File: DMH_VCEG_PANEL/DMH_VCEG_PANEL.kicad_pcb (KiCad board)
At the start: 2 copper layers, 100 x 200 mm, 5 parts, among them J0 Panel_GND_Solder_Wire_Pad

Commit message: 15cm Panel design in progress
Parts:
- added H10: Dec CV, SynthStuff:Pot_Cutout_Tiny_attv_P110KH1, F.Cu at (248.7, 145.7)
- added H11: Sus CV, SynthStuff:Pot_Cutout_Tiny_attv_P110KH1, F.Cu at (274.2, 121.4)
- added H12: Rel CV, SynthStuff:Pot_Cutout_Tiny_attv_P110KH1, F.Cu at (274.2, 145.7)
- added H13: Exp Lin, SynthStuff:Toggle_Switch_TE_Cutout, F.Cu at (243.5, 165.6)
- added H14: Loop, SynthStuff:Toggle_Switch_TE_Cutout, F.Cu at (258.5, 165.6)
- added H15: Att CV, SynthStuff:Jack_6.35mm_Cutout_v3, F.Cu at (33.5, 190.2)
- added H16: Dec CV, SynthStuff:Jack_6.35mm_Cutout_v3, F.Cu at (50.0, 190.2)
- added H17: Sus CV, SynthStuff:Jack_6.35mm_Cutout_v3, F.Cu at (66.5, 190.2)
- added H18: Rel CV, SynthStuff:Jack_6.35mm_Cutout_v3, F.Cu at (83.0, 190.2)
- added H19: Trig, SynthStuff:Jack_6.35mm_Cutout_v3, F.Cu at (83.0, 208.8)
- added H20: Gate, SynthStuff:Jack_6.35mm_Cutout_v3, F.Cu at (66.5, 208.8)
- added H21: Out +, SynthStuff:Jack_6.35mm_Cutout_Output_v6, F.Cu at (33.5, 208.8)
- added H22: Out -, SynthStuff:Jack_6.35mm_Cutout_Output_v6, F.Cu at (50.0, 208.8)
- added H23: SG Out A, SynthStuff:Jack_6.35mm_Cutout_Output_v6, F.Cu at (100.0, 190.2)
- added H24: Att LED, SynthStuff:MountingHole_LED_3mm, F.Cu at (238.7, 175.9)
- added H25: Dec LED, SynthStuff:MountingHole_LED_3mm, F.Cu at (238.7, 181.5)
- added H26: Sus LED, SynthStuff:MountingHole_LED_3mm, F.Cu at (244.3, 175.9)
- added H27: Rel LED, SynthStuff:MountingHole_LED_3mm, F.Cu at (244.3, 181.5)
- added H28: Att LED, SynthStuff:MountingHole_LED_3mm, F.Cu at (249.8, 175.9)
- added H29: Att CV, SynthStuff:Jack_6.35mm_Cutout_v3, F.Cu at (166.5, 190.2)
- added H30: Trig, SynthStuff:Jack_6.35mm_Cutout_v3, F.Cu at (117.0, 208.8)
- added H31: Exp Lin, SynthStuff:Toggle_Switch_TE_Cutout, F.Cu at (273.5, 165.6)
- added H32: Loop, SynthStuff:Toggle_Switch_TE_Cutout, F.Cu at (288.5, 165.6)
- added H33: Dec LED, SynthStuff:MountingHole_LED_3mm, F.Cu at (249.8, 181.5)
- added H34: Dec CV, SynthStuff:Jack_6.35mm_Cutout_v3, F.Cu at (150.0, 190.2)
- added H35: Gate, SynthStuff:Jack_6.35mm_Cutout_v3, F.Cu at (133.5, 208.8)
- added H36: Sus LED, SynthStuff:MountingHole_LED_3mm, F.Cu at (255.4, 175.9)
- added H37: Sus CV, SynthStuff:Jack_6.35mm_Cutout_v3, F.Cu at (133.5, 190.2)
- added H38: Out +, SynthStuff:Jack_6.35mm_Cutout_Output_v6, F.Cu at (166.5, 208.8)
- added H39: Att CV, SynthStuff:Pot_Cutout_Tiny_attv_P110KH1, F.Cu at (299.7, 121.4)
- added H40: Dec CV, SynthStuff:Pot_Cutout_Tiny_attv_P110KH1, F.Cu at (299.7, 145.7)
- added H41: Sus CV, SynthStuff:Pot_Cutout_Tiny_attv_P110KH1, F.Cu at (325.2, 121.4)
- added H42: Rel CV, SynthStuff:Pot_Cutout_Tiny_attv_P110KH1, F.Cu at (325.2, 145.7)
- added H43: Rel LED, SynthStuff:MountingHole_LED_3mm, F.Cu at (255.4, 181.5)
- added H44: Rel CV, SynthStuff:Jack_6.35mm_Cutout_v3, F.Cu at (117.0, 190.2)
- added H45: Out -, SynthStuff:Jack_6.35mm_Cutout_Output_v6, F.Cu at (150.0, 208.8)
- added H46: Attack, SynthStuff:Pot_Cutout_Small, F.Cu at (150.0, 58.5)
- added H47: Decay, SynthStuff:Pot_Cutout_Small, F.Cu at (150.0, 94.0)
- added H48: Sustain, SynthStuff:Pot_Cutout_Small, F.Cu at (150.0, 129.5)
- added H49: Release, SynthStuff:Pot_Cutout_Small, F.Cu at (150.0, 165.0)
- added H5: Attack, SynthStuff:Pot_Cutout_Small, F.Cu at (50.0, 58.5)
- added H50: SG Out B, SynthStuff:Jack_6.35mm_Cutout_Output_v6, F.Cu at (100.0, 208.8)
- added H6: Decay, SynthStuff:Pot_Cutout_Small, F.Cu at (50.0, 94.0)
- added H7: Sustain, SynthStuff:Pot_Cutout_Small, F.Cu at (50.0, 129.5)
- added H8: Release, SynthStuff:Pot_Cutout_Small, F.Cu at (50.0, 165.0)
- added H9: Att CV, SynthStuff:Pot_Cutout_Tiny_attv_P110KH1, F.Cu at (248.7, 121.4)
- moved H1 25.0 mm to (28.5, 33.5)
- moved H2 25.0 mm to (171.5, 33.5)
- moved H3 25.0 mm to (28.5, 226.5)
- moved H4 25.0 mm to (171.5, 226.5)
- moved J0 25.0 mm to (30.0, 130.0)
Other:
- board size 100 x 200 mm -> 150 x 200 mm
- board text added: "VCEG"
- board text removed: "Name"

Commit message: Front panel design in progress
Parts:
- moved H41 212.8 mm to (112.5, 115.5)
- moved H42 212.7 mm to (112.5, 144.0)
- moved H24 205.6 mm to (70.0, 58.5)
- moved H39 197.5 mm to (112.5, 58.5)
- moved H40 196.2 mm to (112.5, 87.0)
- moved H25 191.7 mm to (70.0, 90.5)
- moved H11 186.8 mm to (87.5, 115.5)
- moved H12 186.7 mm to (87.5, 144.0)
- moved H14 182.5 mm to (76.0, 169.0)
- moved H26 182.3 mm to (70.0, 122.5)
- moved H27 176.4 mm to (70.0, 154.5)
- moved H9 173.1 mm to (87.5, 58.5)
- moved H10 171.6 mm to (87.5, 87.0)
- moved H28 167.8 mm to (130.0, 58.5)
- moved H32 164.6 mm to (124.0, 169.0)
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
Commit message: Finished panel design
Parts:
- added H51: MountingHole_Rails, SynthStuff:MountingHole_Rails, F.Cu at (71.5, 33.5)
- added H52: MountingHole_Rails, SynthStuff:MountingHole_Rails, F.Cu at (128.5, 33.5)
- added H53: MountingHole_Rails, SynthStuff:MountingHole_Rails, F.Cu at (71.5, 226.5)
- added H54: MountingHole_Rails, SynthStuff:MountingHole_Rails, F.Cu at (128.5, 226.5)
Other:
- board text added: "A"
- board text added: "B"
- board text added: "Transistor Core"
- board text removed: "TYPE"

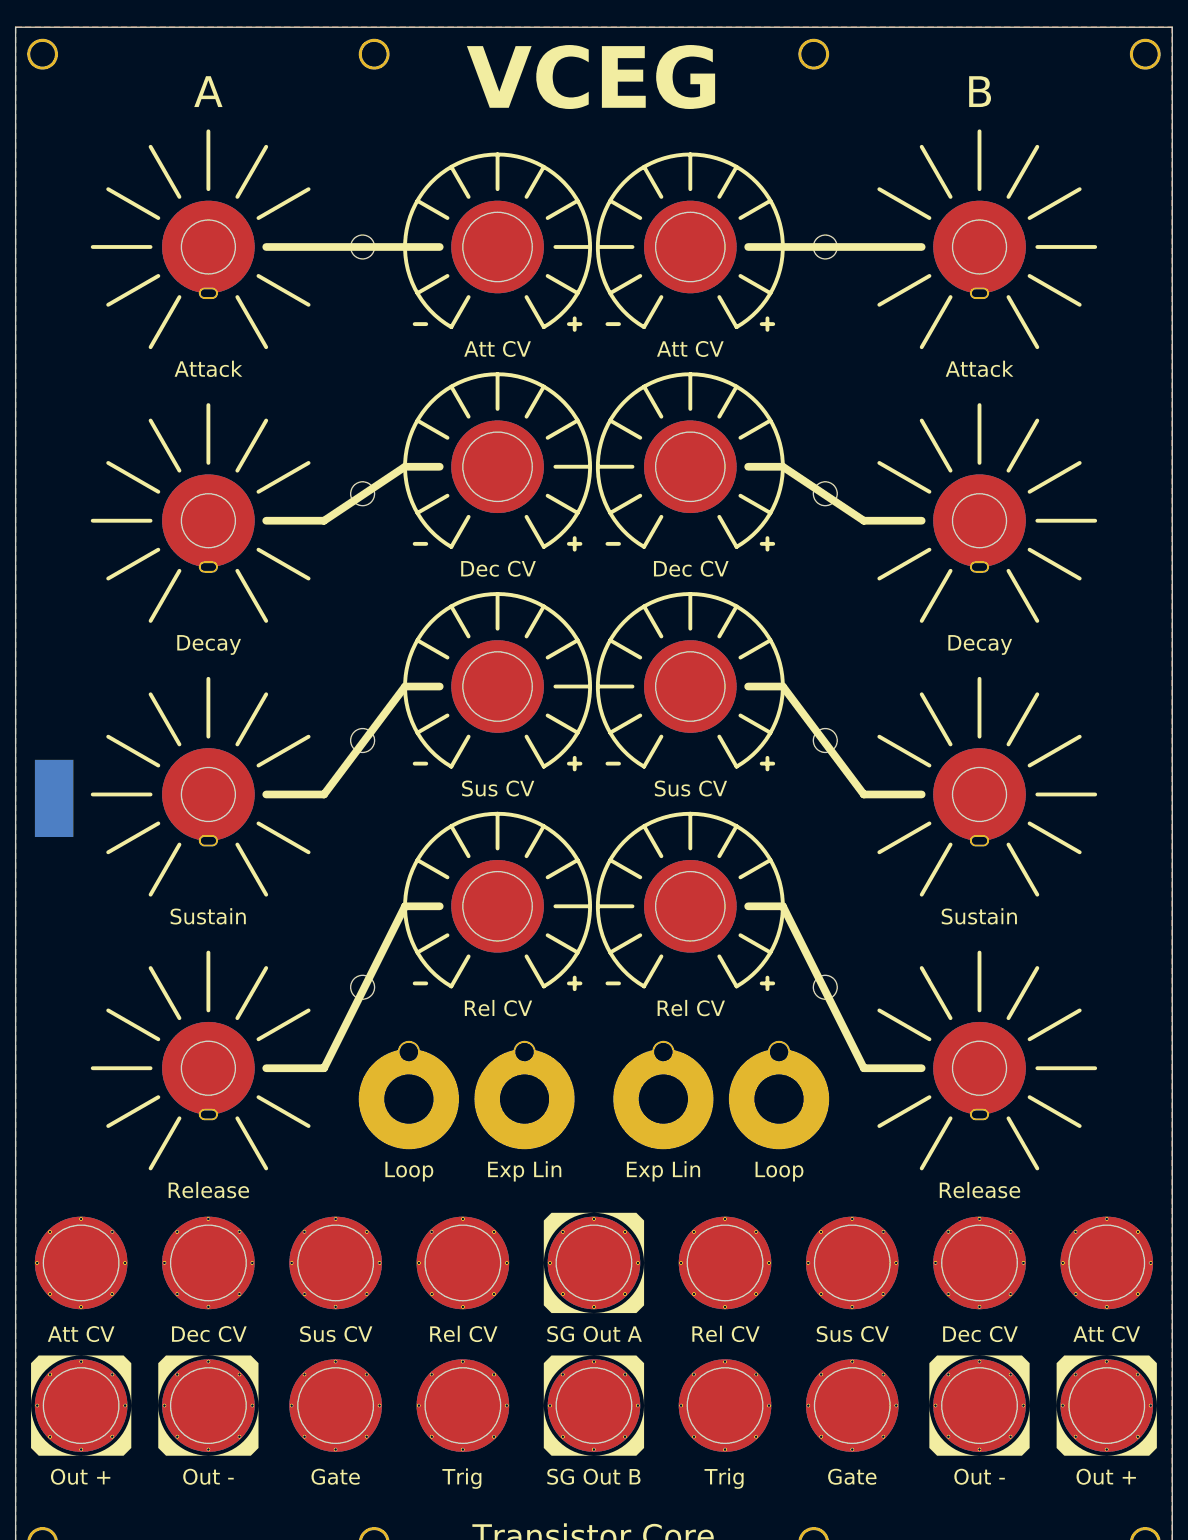
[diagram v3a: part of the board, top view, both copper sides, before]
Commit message: Added amplitude CV input and pot
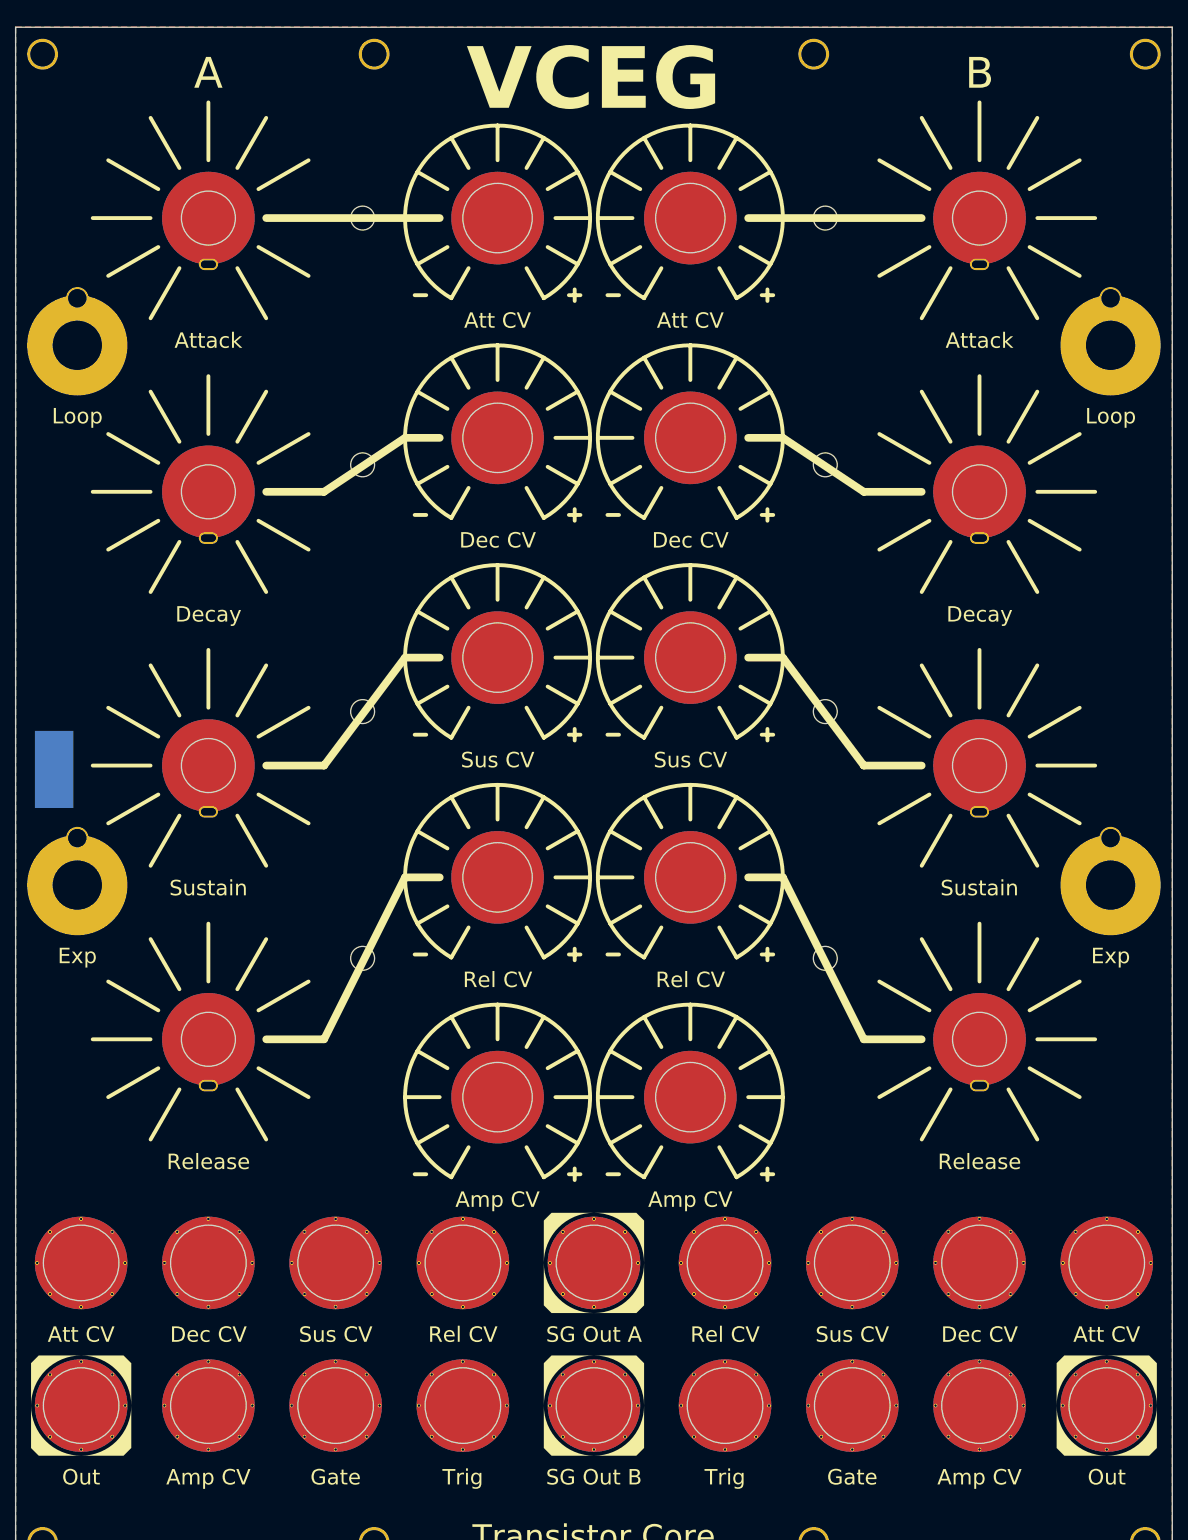
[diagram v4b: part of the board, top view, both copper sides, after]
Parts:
- added H55: Amp CV, SynthStuff:Pot_Cutout_Tiny_attv_P110KH1, F.Cu at (87.5, 168.8)
- added H56: Amp CV, SynthStuff:Pot_Cutout_Tiny_attv_P110KH1, F.Cu at (112.5, 168.8)
- H13, H31: value Exp Lin -> Exp
- H21, H38: value Out + -> Out
- H22, H45: value Out - -> Amp CV; footprint SynthStuff:Jack_6.35mm_Cutout_Output_v6 -> SynthStuff:Jack_6.35mm_Cutout_v3
- moved H14 106.8 mm to (33.0, 71.2)
- moved H32 106.8 mm to (167.0, 71.2)
- moved H13 64.3 mm to (33.0, 141.2)
- moved H31 64.3 mm to (167.0, 141.2)
- moved H10 3.75 mm to (87.5, 83.2)
- moved H11 3.75 mm to (87.5, 111.8)
- moved H12 3.75 mm to (87.5, 140.2)
- moved H24 3.75 mm to (70.0, 54.8)
- moved H25 3.75 mm to (70.0, 86.8)
- moved H26 3.75 mm to (70.0, 118.8)
- moved H27 3.75 mm to (70.0, 150.8)
- moved H28 3.75 mm to (130.0, 54.8)
- moved H33 3.75 mm to (130.0, 86.8)
- moved H36 3.75 mm to (130.0, 118.8)
- moved H39 3.75 mm to (112.5, 54.8)
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
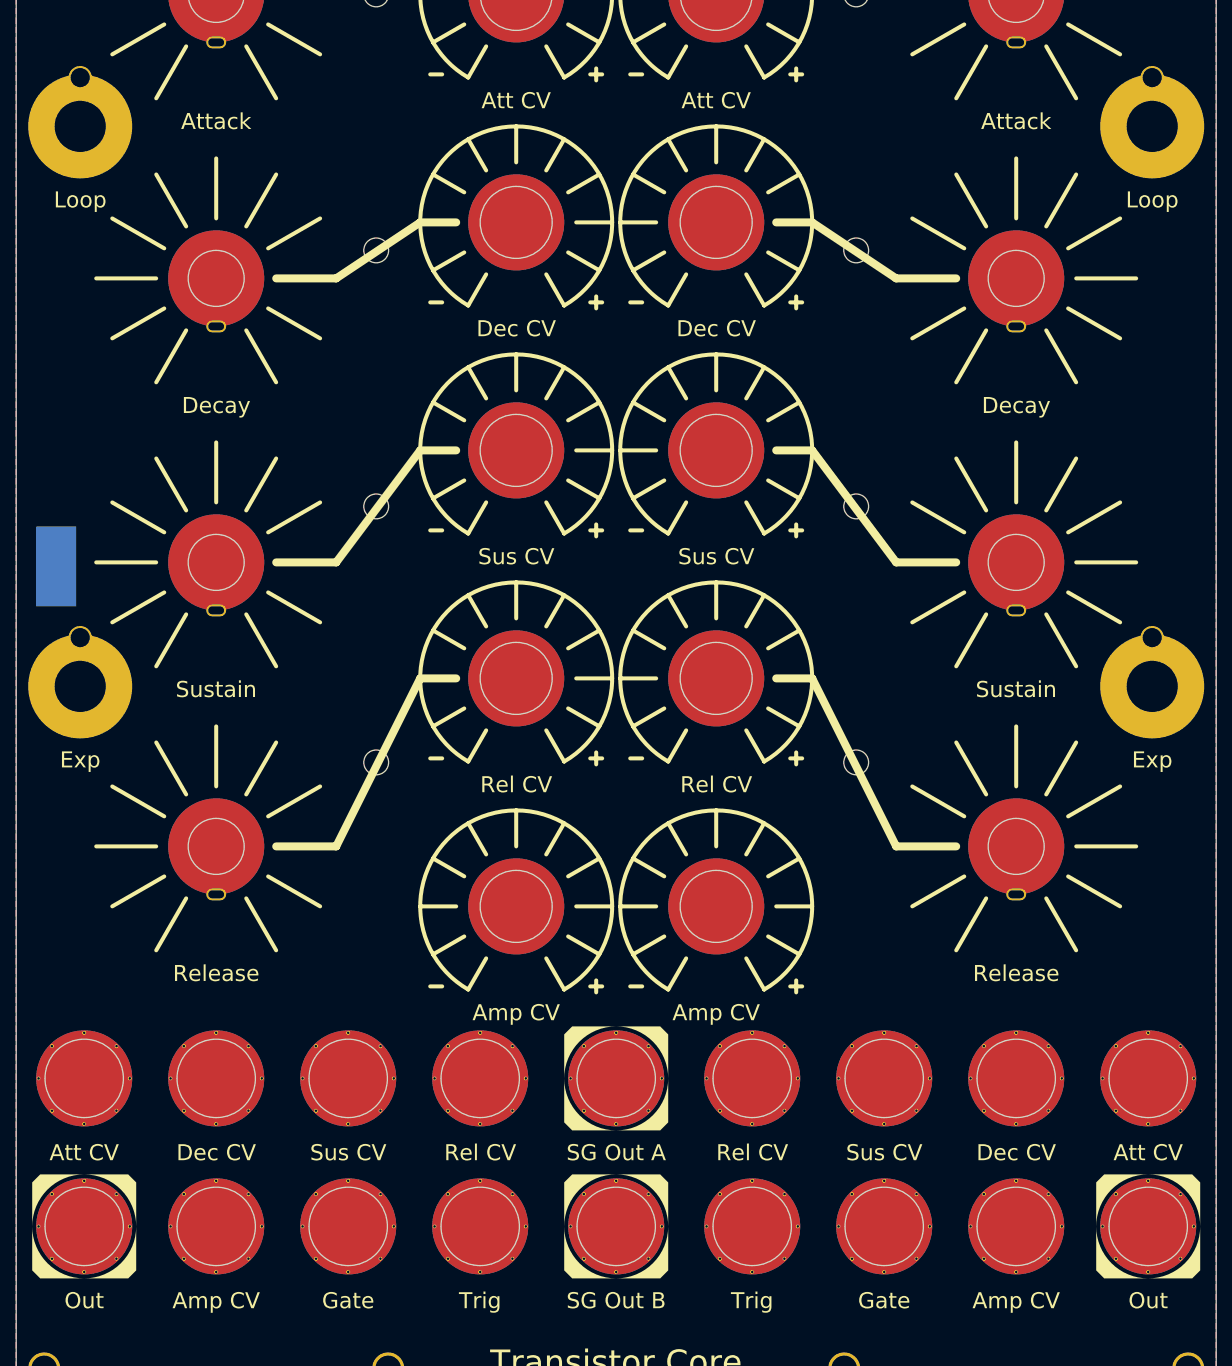
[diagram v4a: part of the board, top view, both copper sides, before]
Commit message: Added more features
- Amp offset switch
- Re-added Out -
- Added Out R
- Rearranged positions to make everything fit
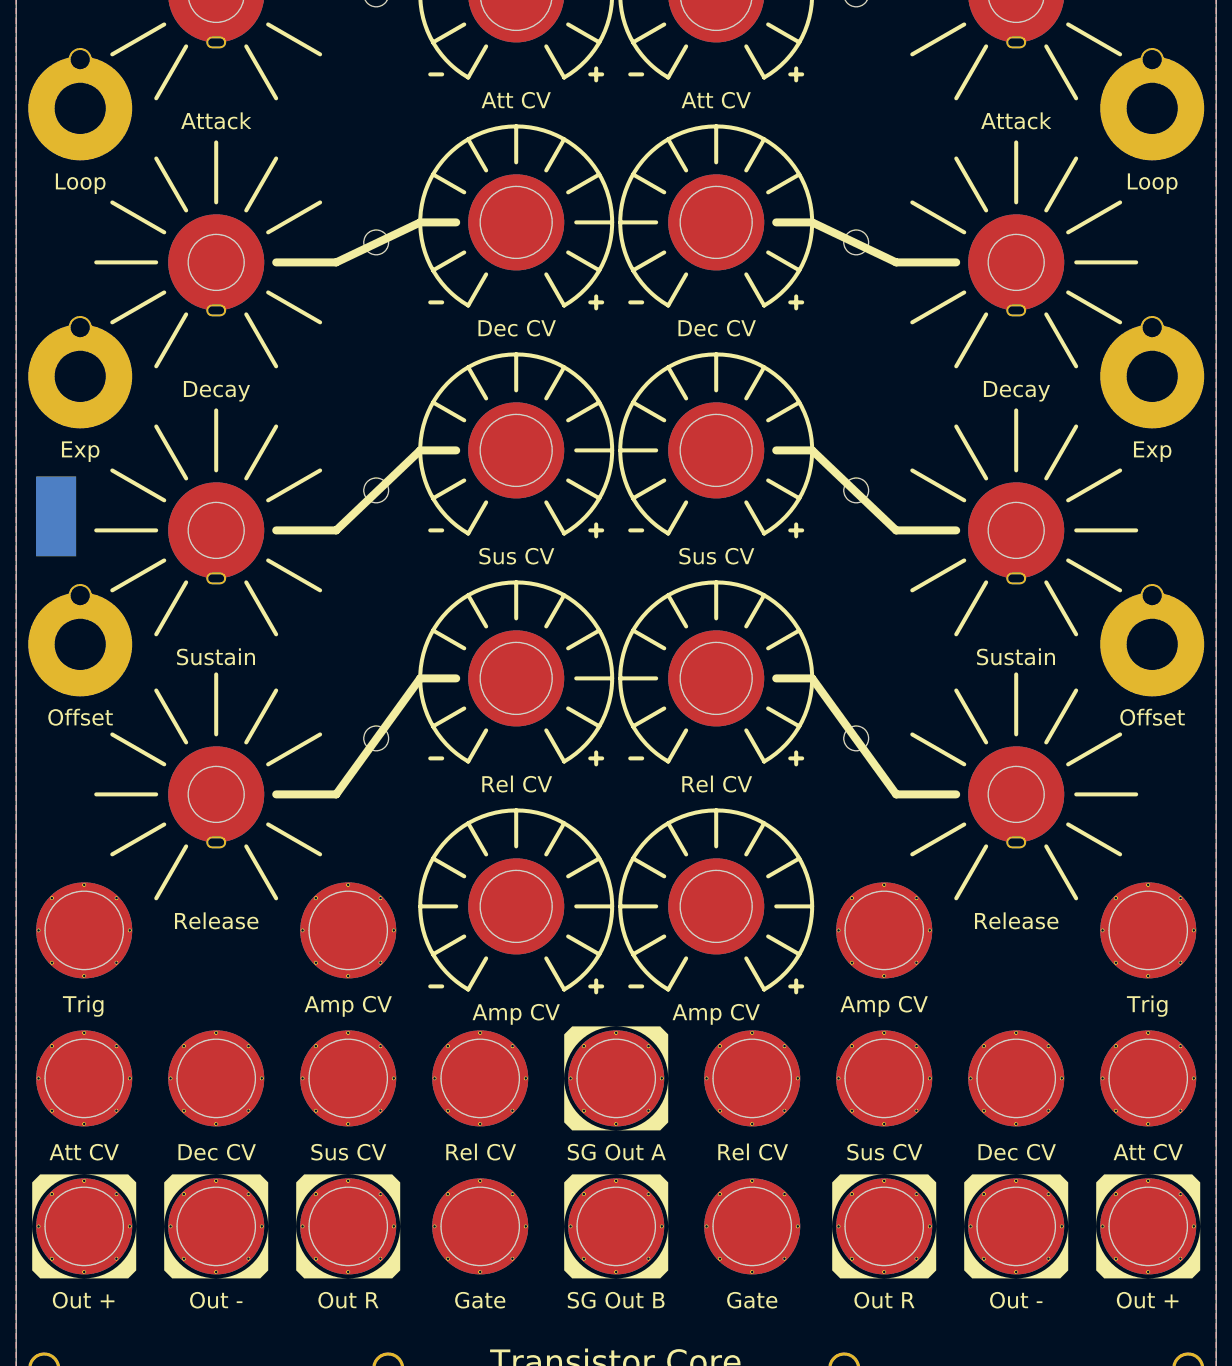
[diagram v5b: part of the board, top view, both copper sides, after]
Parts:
- added H57: Offset, SynthStuff:Toggle_Switch_TE_Cutout, F.Cu at (167.0, 136.0)
- added H58: Offset, SynthStuff:Toggle_Switch_TE_Cutout, F.Cu at (33.0, 136.0)
- added H59: Out -, SynthStuff:Jack_6.35mm_Cutout_Output_v6, F.Cu at (50.0, 208.8)
- added H60: Out R, SynthStuff:Jack_6.35mm_Cutout_Output_v6, F.Cu at (66.5, 208.8)
- added H61: Out R, SynthStuff:Jack_6.35mm_Cutout_Output_v6, F.Cu at (133.5, 208.8)
- added H62: Out -, SynthStuff:Jack_6.35mm_Cutout_Output_v6, F.Cu at (150.0, 208.8)
- H21, H38: value Out -> Out +
- moved H19 61.8 mm to (33.5, 171.8)
- moved H30 61.8 mm to (166.5, 171.8)
- moved H22 40.5 mm to (66.5, 171.8)
- moved H45 40.5 mm to (133.5, 171.8)
- moved H13 38.8 mm to (33.0, 102.5)
- moved H31 38.8 mm to (167.0, 102.5)
- moved H20 16.5 mm to (83.0, 208.8)
- moved H35 16.5 mm to (117.0, 208.8)
- moved H49 6.50 mm to (150.0, 154.8)
- moved H8 6.50 mm to (50.0, 154.8)
- moved J0 6.25 mm to (30.0, 120.0)
- moved H48 4.00 mm to (150.0, 121.8)
- moved H7 4.00 mm to (50.0, 121.8)
- moved H27 3.00 mm to (70.0, 147.8)
- moved H43 3.00 mm to (130.0, 147.8)
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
